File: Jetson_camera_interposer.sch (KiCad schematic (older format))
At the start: 25 parts, among them J1 QSH-060-01-L-D-A, J10 JETSON_1V8, J11 VDD_3V3, J12 VDD_SYS, J13 VDD_CAM_FQ_HV_CAM, J14 CAM_AF_PWDN, J15 CAM_FLASH_EN, J16 JETSON_1V2, J17 VDD_IR, J18 IR_READY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

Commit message: placed jumpers
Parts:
- removed GND4, I2C_CLK2, I2C_DAT2: TestP, TX2_Footprints:test_point, symbol TX2_Symbols:TEST_1P
- removed J26, J3: Conn_01x01, TX2_Footprints:ground_probe, symbol TX2_Symbols:Conn_01x01
- removed J7: Conn_01x01, Pin_Headers:Pin_Header_Straight_1x01_Pitch2.54mm, symbol Connector_Generic:Conn_01x01
- added J? (x4): GND, Pin_Headers:Pin_Header_Straight_1x01_Pitch2.54mm, symbol Connector_Generic:Conn_01x01
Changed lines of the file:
@@
 Text Label 7050 2500 0    60   ~ 0
 CSI0_D1_N
-$Comp
-L TX2_Symbols:Conn_01x01 J3
-U 1 1 5A60149C
-P 11850 7800
-F 0 "J3" H 11850 7900 50  0000 C CNN
-F 1 "Conn_01x01" H 11850 7700 50  0001 C CNN
-F 2 "TX2_Footprints:ground_probe" H 11850 7800 50  0001 C CNN
-F 3 "" H 11850 7800 50  0001 C CNN
-	1    11850 7800
-	1    0    0    -1
-$EndComp
 Text Notes 11400 7550 0    60   ~ 0
 Ground pads
@@
 Connection ~ 11450 8200
 Wire Wire Line
-	11450 8200 11650 8200
-Wire Wire Line
 	11650 7800 11450 7800
 Wire Wire Line
@@
 Wire Wire Line
 	6850 6100 8100 6100
-$Comp
-L TX2_Symbols:TEST_1P I2C_DAT2
-U 1 1 5BA2560B
-P 5700 7200
-F 0 "I2C_DAT2" V 5650 7400 50  0000 C CNN
-F 1 "TestP" V 5700 7550 50  0001 C CNN
-F 2 "TX2_Footprints:test_point" H 5900 7200 50  0001 C CNN
-F 3 "" H 5900 7200 50  0001 C CNN
-	1    5700 7200
-	0    -1   -1   0
-$EndComp
-$Comp
-L TX2_Symbols:TEST_1P I2C_CLK2
-U 1 1 5BA256F4
-P 6000 7100
-F 0 "I2C_CLK2" V 6050 7050 50  0000 C CNN
-F 1 "TestP" V 6000 7350 50  0001 C CNN
-F 2 "TX2_Footprints:test_point" H 6200 7100 50  0001 C CNN
-F 3 "" H 6200 7100 50  0001 C CNN
-	1    6000 7100
-	0    -1   -1   0
-$EndComp
 Wire Wire Line
 	11750 8500 11450 8500
@@
 Wire Wire Line
 	11450 8500 11450 8700
-$Comp
-L TX2_Symbols:TEST_1P GND4
-U 1 1 5BA2777D
-P 11750 8500
-F 0 "GND4" V 11750 8800 50  0000 C CNN
-F 1 "TestP" V 11850 8650 50  0001 C CNN
-F 2 "TX2_Footprints:test_point" H 11950 8500 50  0001 C CNN
-F 3 "" H 11950 8500 50  0001 C CNN
-	1    11750 8500
-	0    1    1    0
-$EndComp
-$Comp
-L TX2_Symbols:Conn_01x01 J26
-U 1 1 5B81DEE2
-P 11850 8200
-F 0 "J26" H 11850 8300 50  0000 C CNN
-F 1 "Conn_01x01" H 11850 8100 50  0000 C CNN
-F 2 "TX2_Footprints:ground_probe" H 11850 8200 50  0001 C CNN
-F 3 "" H 11850 8200 50  0001 C CNN
-	1    11850 8200
-	1    0    0    -1
-$EndComp
 Text Label 1250 1800 0    60   ~ 0
 CSI0_D0_P
@@
 Text Label 10000 4500 0    60   ~ 0
 DVDD_CAM_LV
-$Comp
-L Connector_Generic:Conn_01x01 J7
-U 1 1 617A3BD0
-P 11900 8700
-F 0 "J7" H 11980 8742 50  0000 L CNN
-F 1 "Conn_01x01" H 11980 8651 50  0000 L CNN
-F 2 "Pin_Headers:Pin_Header_Straight_1x01_Pitch2.54mm" H 11900 8700 50  0001 C CNN
-F 3 "~" H 11900 8700 50  0001 C CNN
-	1    11900 8700
-	1    0    0    -1
-$EndComp
 Text Label 13550 5800 0    60   ~ 0
 DVDD_CAM_LV
@@
 Text Label 13550 6200 0    60   ~ 0
 JETSON_1V8
+Wire Wire Line
+	11450 8200 11650 8200
+$Comp
+L Connector_Generic:Conn_01x01 J?
+U 1 1 61BA09C5
+P 11850 7800
+F 0 "J?" H 11930 7842 50  0000 L CNN
+F 1 "GND" H 12050 7800 50  0000 L CNN
+F 2 "Pin_Headers:Pin_Header_Straight_1x01_Pitch2.54mm" H 11850 7800 50  0001 C CNN
+F 3 "~" H 11850 7800 50  0001 C CNN
+	1    11850 7800
+	1    0    0    -1
+$EndComp
+$Comp
+L Connector_Generic:Conn_01x01 J?
+U 1 1 61BA0DC5
+P 11850 8200
+F 0 "J?" H 11930 8242 50  0000 L CNN
+F 1 "GND" H 12000 8200 50  0000 L CNN
+F 2 "Pin_Headers:Pin_Header_Straight_1x01_Pitch2.54mm" H 11850 8200 50  0001 C CNN
+F 3 "~" H 11850 8200 50  0001 C CNN
+	1    11850 8200
+	1    0    0    -1
+$EndComp
+$Comp
+L Connector_Generic:Conn_01x01 J?
+U 1 1 61BA107F
+P 11950 8500
+F 0 "J?" H 12030 8542 50  0000 L CNN
+F 1 "GND" H 12150 8550 50  0000 L CNN
+F 2 "Pin_Headers:Pin_Header_Straight_1x01_Pitch2.54mm" H 11950 8500 50  0001 C CNN
+F 3 "~" H 11950 8500 50  0001 C CNN
+	1    11950 8500
+	1    0    0    -1
+$EndComp
+$Comp
+L Connector_Generic:Conn_01x01 J?
+U 1 1 61BA1316
+P 11900 8700
+F 0 "J?" H 11980 8742 50  0000 L CNN
+F 1 "GND" H 12100 8700 50  0000 L CNN
+F 2 "Pin_Headers:Pin_Header_Straight_1x01_Pitch2.54mm" H 11900 8700 50  0001 C CNN
+F 3 "~" H 11900 8700 50  0001 C CNN
+	1    11900 8700
+	1    0    0    -1
+$EndComp
 $EndSCHEMATC

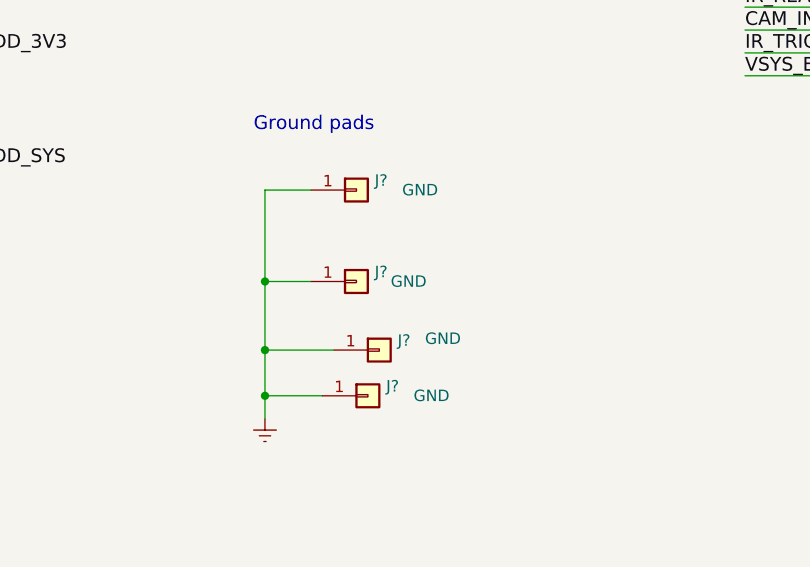
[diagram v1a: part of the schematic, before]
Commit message: placed debug connectors
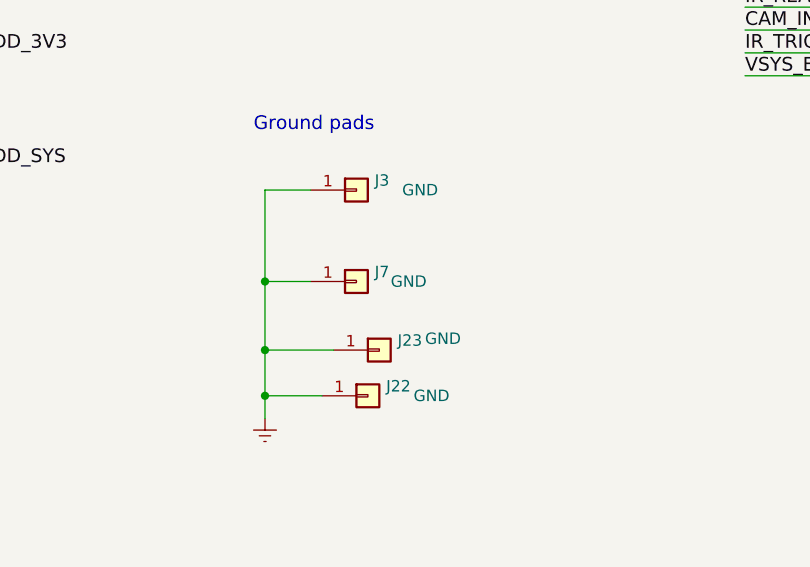
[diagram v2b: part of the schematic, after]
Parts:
- gave numbers to parts that had none: 4
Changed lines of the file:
@@
 	11450 8200 11650 8200
 $Comp
-L Connector_Generic:Conn_01x01 J?
+L Connector_Generic:Conn_01x01 J3
 U 1 1 61BA09C5
 P 11850 7800
-F 0 "J?" H 11930 7842 50  0000 L CNN
+F 0 "J3" H 11930 7842 50  0000 L CNN
 F 1 "GND" H 12050 7800 50  0000 L CNN
 F 2 "Pin_Headers:Pin_Header_Straight_1x01_Pitch2.54mm" H 11850 7800 50  0001 C CNN
@@
 $EndComp
 $Comp
-L Connector_Generic:Conn_01x01 J?
+L Connector_Generic:Conn_01x01 J7
 U 1 1 61BA0DC5
 P 11850 8200
-F 0 "J?" H 11930 8242 50  0000 L CNN
+F 0 "J7" H 11930 8242 50  0000 L CNN
 F 1 "GND" H 12000 8200 50  0000 L CNN
 F 2 "Pin_Headers:Pin_Header_Straight_1x01_Pitch2.54mm" H 11850 8200 50  0001 C CNN
@@
 $EndComp
 $Comp
-L Connector_Generic:Conn_01x01 J?
+L Connector_Generic:Conn_01x01 J23
 U 1 1 61BA107F
 P 11950 8500
-F 0 "J?" H 12030 8542 50  0000 L CNN
+F 0 "J23" H 12030 8542 50  0000 L CNN
 F 1 "GND" H 12150 8550 50  0000 L CNN
 F 2 "Pin_Headers:Pin_Header_Straight_1x01_Pitch2.54mm" H 11950 8500 50  0001 C CNN
@@
 $EndComp
 $Comp
-L Connector_Generic:Conn_01x01 J?
+L Connector_Generic:Conn_01x01 J22
 U 1 1 61BA1316
 P 11900 8700
-F 0 "J?" H 11980 8742 50  0000 L CNN
+F 0 "J22" H 11980 8742 50  0000 L CNN
 F 1 "GND" H 12100 8700 50  0000 L CNN
 F 2 "Pin_Headers:Pin_Header_Straight_1x01_Pitch2.54mm" H 11900 8700 50  0001 C CNN

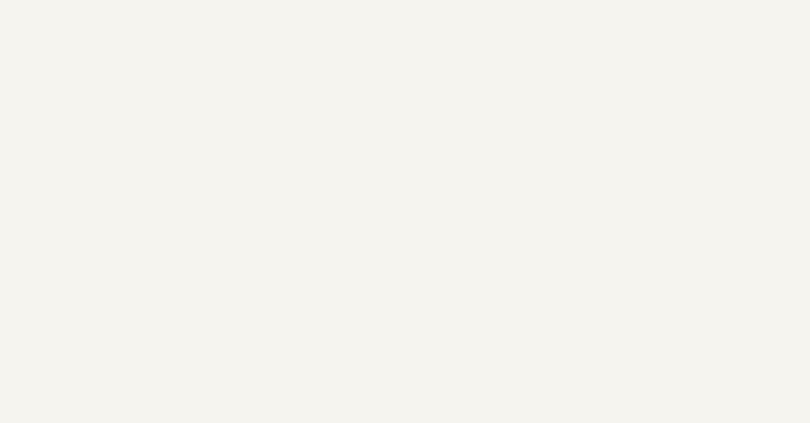
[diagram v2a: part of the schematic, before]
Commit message: added mounting holes
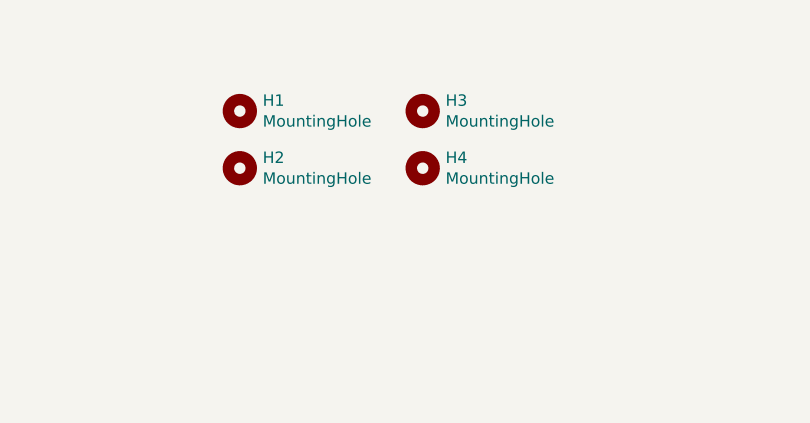
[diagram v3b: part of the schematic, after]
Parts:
- added H1, H2, H3, H4: MountingHole, Mounting_Holes:MountingHole_2.2mm_M2, symbol Mechanical:MountingHole
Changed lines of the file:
@@
+	1    0    0    -1
+$EndComp
+$Comp
+L Mechanical:MountingHole H1
+U 1 1 61660B00
+P 12600 1450
+F 0 "H1" H 12700 1496 50  0000 L CNN
+F 1 "MountingHole" H 12700 1405 50  0000 L CNN
+F 2 "Mounting_Holes:MountingHole_2.2mm_M2" H 12600 1450 50  0001 C CNN
+F 3 "~" H 12600 1450 50  0001 C CNN
+	1    12600 1450
+	1    0    0    -1
+$EndComp
+$Comp
+L Mechanical:MountingHole H3
+U 1 1 61662E08
+P 13400 1450
+F 0 "H3" H 13500 1496 50  0000 L CNN
+F 1 "MountingHole" H 13500 1405 50  0000 L CNN
+F 2 "Mounting_Holes:MountingHole_2.2mm_M2" H 13400 1450 50  0001 C CNN
+F 3 "~" H 13400 1450 50  0001 C CNN
+	1    13400 1450
+	1    0    0    -1
+$EndComp
+$Comp
+L Mechanical:MountingHole H4
+U 1 1 61663198
+P 13400 1700
+F 0 "H4" H 13500 1746 50  0000 L CNN
+F 1 "MountingHole" H 13500 1655 50  0000 L CNN
+F 2 "Mounting_Holes:MountingHole_2.2mm_M2" H 13400 1700 50  0001 C CNN
+F 3 "~" H 13400 1700 50  0001 C CNN
+	1    13400 1700
+	1    0    0    -1
+$EndComp
+$Comp
+L Mechanical:MountingHole H2
+U 1 1 61663337
+P 12600 1700
+F 0 "H2" H 12700 1746 50  0000 L CNN
+F 1 "MountingHole" H 12700 1655 50  0000 L CNN
+F 2 "Mounting_Holes:MountingHole_2.2mm_M2" H 12600 1700 50  0001 C CNN
+F 3 "~" H 12600 1700 50  0001 C CNN
+	1    12600 1700
 	1    0    0    -1
 $EndComp
